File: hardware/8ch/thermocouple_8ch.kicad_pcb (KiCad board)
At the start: 4 copper layers, 250 x 140 mm, 209 parts, among them J1 24V_INPUT, J2 LCD_16x2_HEADER, J3 RELAY_COM_NO_NC, J4 RS485_A_B_GND_SHIELD, J5 AVR_ISP, J6 MCU_EXPANSION, K1 G5LE-1 DC24, Q1 BSS131, SW1 NEXT, SW2 UP, SW3 DOWN, SW4 SET, SW5 ACK, U1 ATmega32A-PU, U10 ISO7760DWR, U11 ISO7761DWR, U12 IA0505S, U13 LP2985-3.3, U14 LM5164DDAR, U15 ADM2587EBRWZ, U2 MAX31856MUD+, U3 MAX31856MUD+, U4 MAX31856MUD+, U5 MAX31856MUD+, U6 MAX31856MUD+, U7 MAX31856MUD+, U8 MAX31856MUD+, U9 MAX31856MUD+, Y1 8MHz 20pF

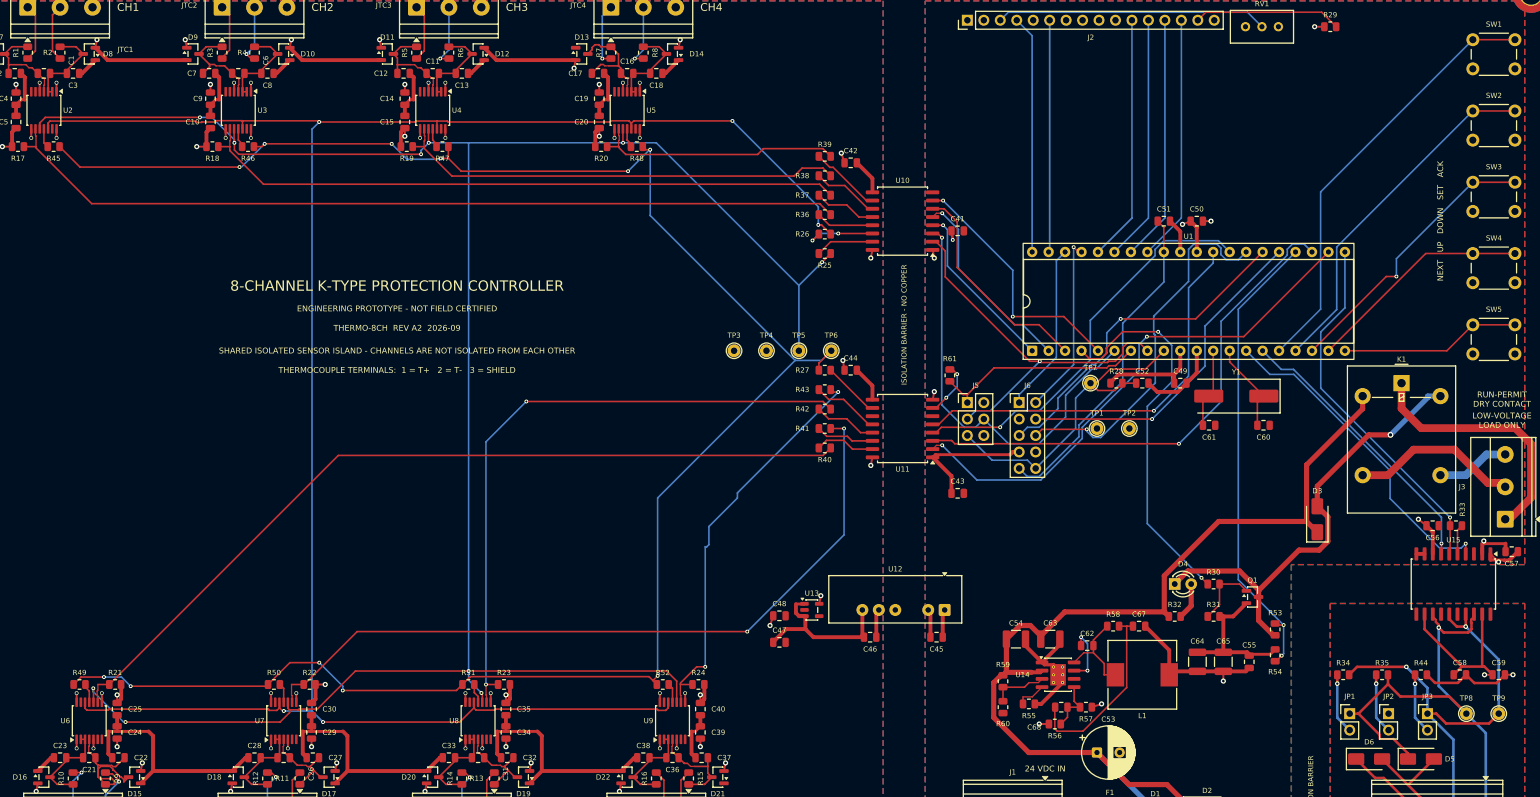
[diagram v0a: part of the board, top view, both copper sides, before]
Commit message: U14 thermal vias 0.3 mm (0023, supersedes 0017); C41.1 fixed via; REV A2 re-routed
Smallest hole on the board is now 0.3 mm. Board fully generated, no hand edits.
validate.ps1 2026-09-28 01:43: ERC 0/0, netlist IDENTICAL 202/163/647,
DRC 0/0/0/0; check_board.py all 6 ok.

Co-Authored-By: Claude Opus 5.5 <noreply@anthropic.com>
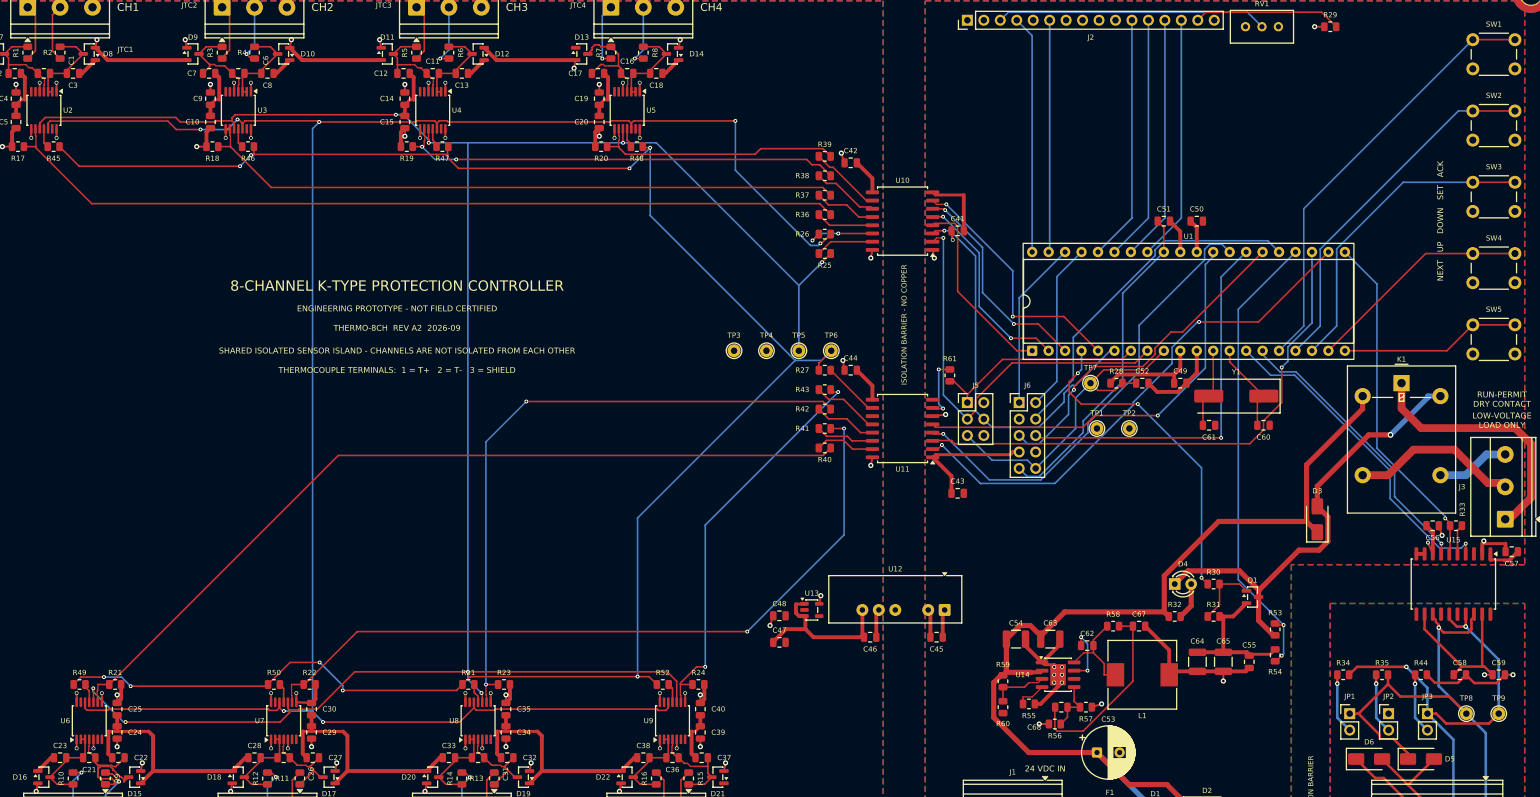
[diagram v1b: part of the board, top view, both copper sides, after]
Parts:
- U14: footprint Package_SO:SOIC-8-1EP_3.9x4.9mm_P1.27mm_EP2.41x3.3mm_ThermalVias -> Package_SO:SOIC-8-1EP_3.9x4.9mm_P1.27mm_EP2.41x3.3mm
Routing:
- net /RUN_PERMIT: track 59.8 -> 50.7 mm, vias 2 -> 3
- net /GND_CTRL: track 77.2 -> 86.2 mm, vias 4 -> 9
- net /CS7_CTRL: track 63.0 -> 70.4 mm
- net /MCU/BTN_DOWN: track 43.7 -> 49.1 mm, vias 1 -> 0
- net /MOSI_SENS: track 322.3 -> 327.6 mm, vias 5 -> 7
- net /MOSI_CTRL: track 65.6 -> 60.5 mm
- net /SCK_CTRL: track 60.4 -> 64.6 mm
- net /RS485_DE: track 56.4 -> 53.4 mm
- net /CS6_CTRL: track 79.8 -> 82.7 mm
- net /CS1_CTRL: track 26.7 -> 29.5 mm, vias 1 -> 0
- net /MCU/SPARE_PC3: track 51.9 -> 54.2 mm, vias 1 -> 0
- net /SCK_SENS: track 346.0 -> 343.8 mm, vias 10 -> 8
- net /MISO_SENS: track 308.5 -> 306.5 mm, vias 11 -> 9
- net /MCU/SPARE_PA3: track 27.9 -> 26.2 mm, vias 1 -> 0
- net /MCU/SPARE_PC5: track 57.3 -> 59.0 mm
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
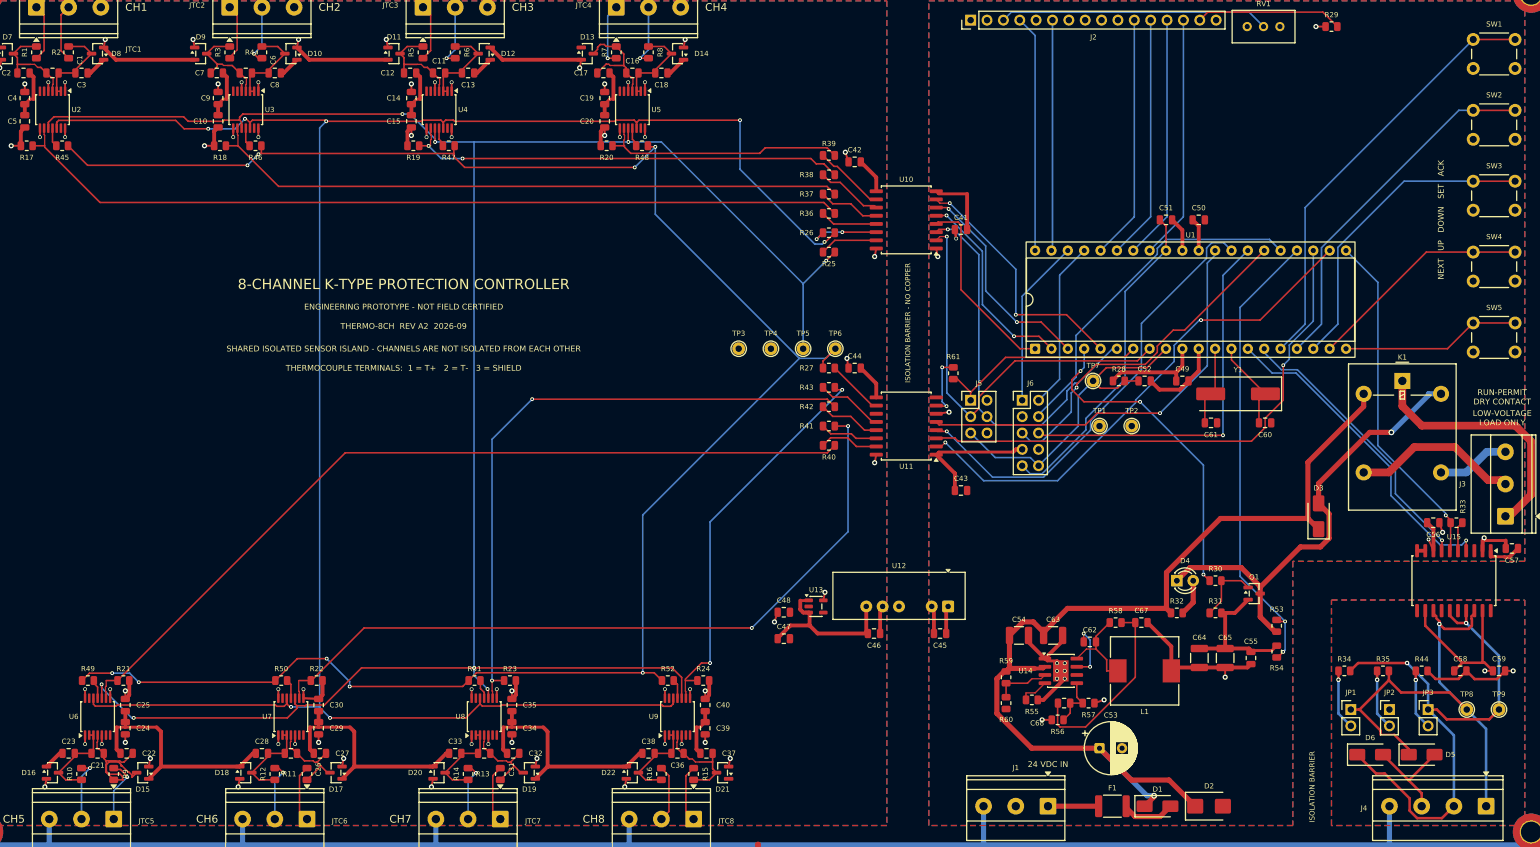
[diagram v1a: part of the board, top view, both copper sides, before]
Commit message: P0: U14 power stage drawn by the generator (0026), via re-drill after SES import (I-075), unsafe ACK fixed (I-073)
- route.py restores a 0.15 mm ring on the 41 vias the SES import re-drilled
  to 0.4 mm; apply_rules.py min_via_annular_width 0.15 so DRC catches it
- board/powerstage.py + placement: C63/C54 at U14.1-2, SW one 1.0 mm track
  to L1, BST 3 mm; protected in the DSN. VIN-C63 19.5 -> 3.5 mm
- protection.c: a recovered save fault passes the normal ACK checks; 5
  regression tests (sub-agent, reviewed); version REVA2; CI uses reva2
validate.ps1 2026-10-01 00:44: ERC 0/0, netlist IDENTICAL 202/163/647,
DRC 0/0/0/0; check_board all ok; .drl: six 0.3 mm at U14; build.ps1 PASS.

Co-Authored-By: Claude Opus 5.5 <noreply@anthropic.com>
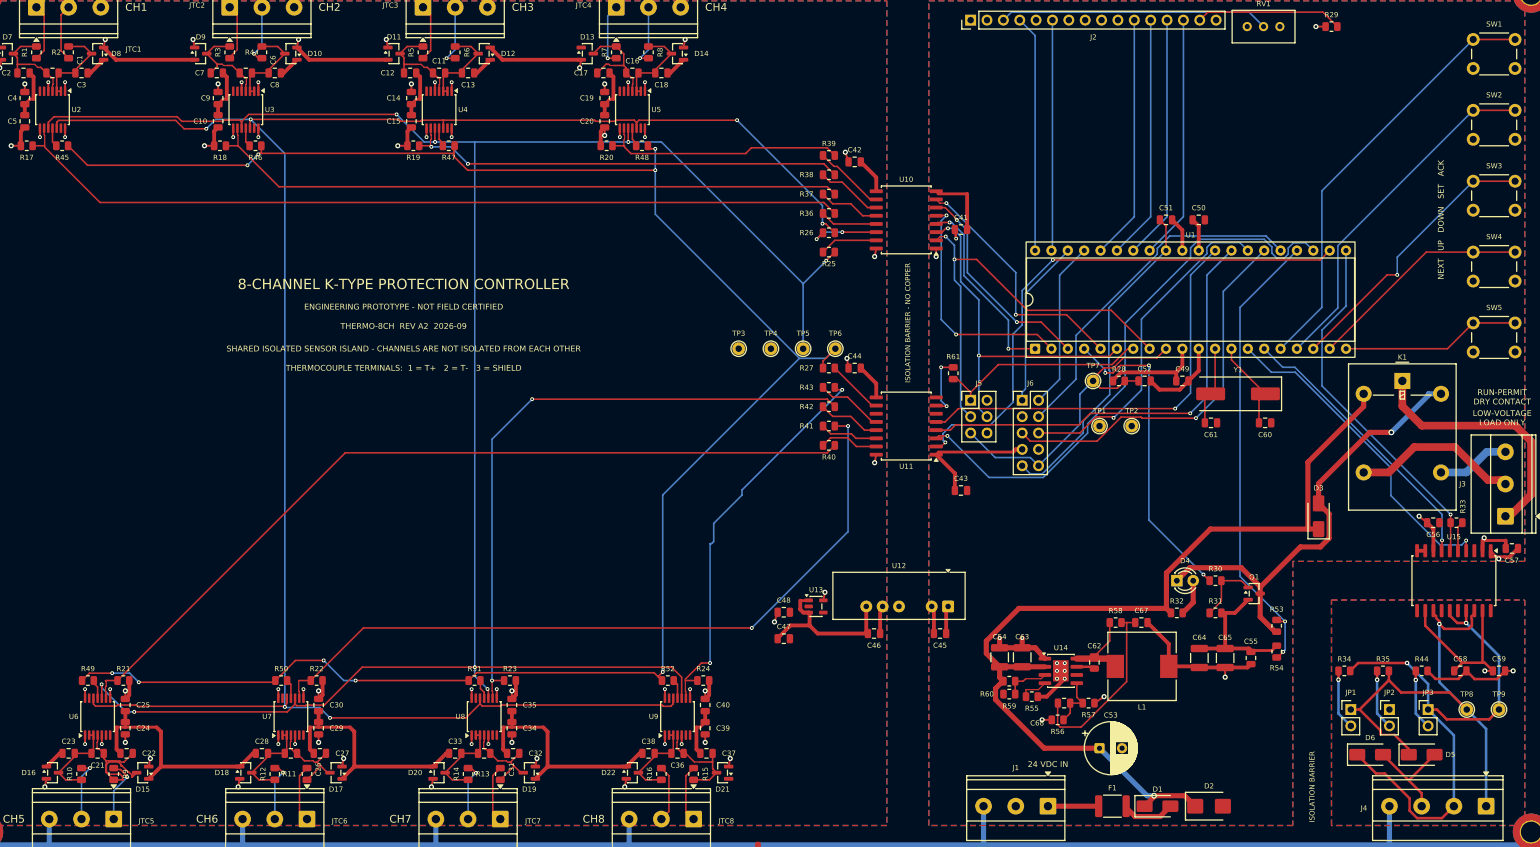
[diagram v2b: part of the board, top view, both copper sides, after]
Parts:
- moved C63 5.88 mm to (166.0, 107.9), turned to 90 degrees
- moved C54 4.53 mm to (162.5, 107.9), turned to 90 degrees
- moved C62 3.28 mm to (177.2, 108.7), turned to 90 degrees
- moved R60 1.49 mm to (164.0, 113.6), turned to 180 degrees
- moved L1 0.81 mm to (184.6, 109.3)
- moved R59 0.78 mm to (164.0, 111.6), turned to 0 degrees
- moved R55 0.50 mm to (167.5, 114.0)
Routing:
- net /+24V_PROT: track 155.1 -> 145.4 mm
- net /MCU/SPARE_PC5: track 59.0 -> 52.4 mm
- net /MCU/SPARE_PC4: track 52.9 -> 59.5 mm
- net /POWER/BST_5V: track 8.94 -> 3.01 mm, vias 2 -> 0
- net /CS2_CTRL: track 31.3 -> 37.1 mm
- net /MCU/BTN_DOWN: track 49.1 -> 43.7 mm, vias 0 -> 1
- net /CS6_CTRL: track 82.7 -> 88.0 mm
- net /MOSI_CTRL: track 60.5 -> 56.2 mm, vias 1 -> 2
- net /CS5_CTRL: track 80.3 -> 84.3 mm
- net /MISO_SENS: track 306.5 -> 303.3 mm
- net /RS485_DE: track 53.4 -> 56.4 mm
- net /GND_CTRL: track 86.2 -> 83.4 mm, vias 9 -> 10
- net /SCK_CTRL: track 64.6 -> 67.3 mm, vias 1 -> 2
- net /POWER/SW_5V: track 14.4 -> 12.2 mm
- net /CS7_CTRL: track 70.4 -> 68.4 mm
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
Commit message: Image guard refuses unapproved images (I-082); refused-ACK reason on LCD (I-088); every BOM line sourced (0027)
- program.ps1 exits 2 on any image but thermo_8ch_max31856.hex (run: legacy image -> exit 2, no avrdude)
- NO ACK CHn HOT/FAULT status after a refused ACK; permit logic unchanged
- LCSC codes: MAX31856MUD+T, LP2985, ADM2587E, ATmega32A-PU, 3296W
- substitutes: K1 G5LE-14 DC24, C53 Rubycon 100YXF22; U12 XP IA0505S from DigiKey
- technician fits THT; 3 boards
build.ps1 exit 0, 3 suites PASS; validate.ps1 01:25 ERC 0/0, IDENTICAL, DRC 0/0/0/0.

Co-Authored-By: Claude Opus 5.5 <noreply@anthropic.com>
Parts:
- K1: value G5LE-1 DC24 -> G5LE-14 DC24
